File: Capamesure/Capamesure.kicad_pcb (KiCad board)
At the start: 2 copper layers, 75 x 48 mm, 61 parts, among them Q1 MMBT3904, Q2 MMBT3904, Q3 MMBT3906, Q4 MMBT3906, Q5 MMBT3904, Q6 MMBT3904, Q7 MMBT3904, U1 AZ1117-5.0

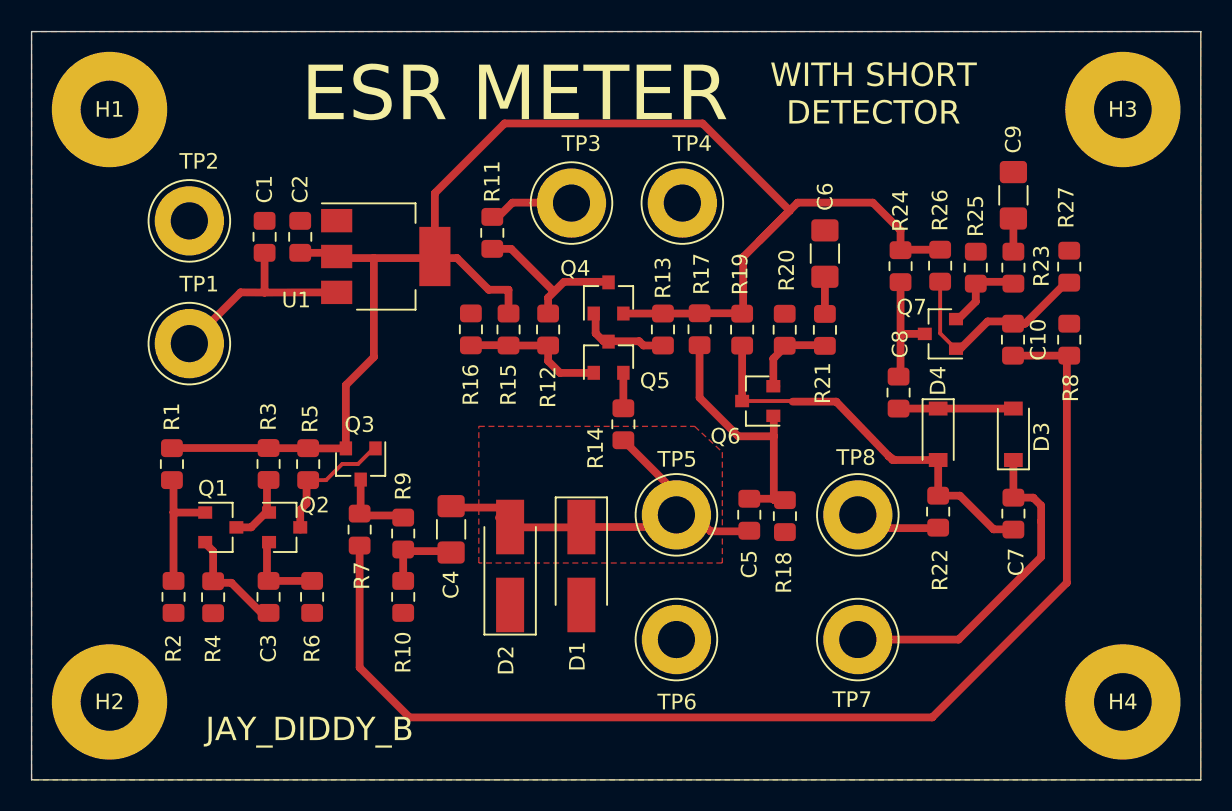
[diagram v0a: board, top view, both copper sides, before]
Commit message: Capacitor & Resistoir changes
changed footprint
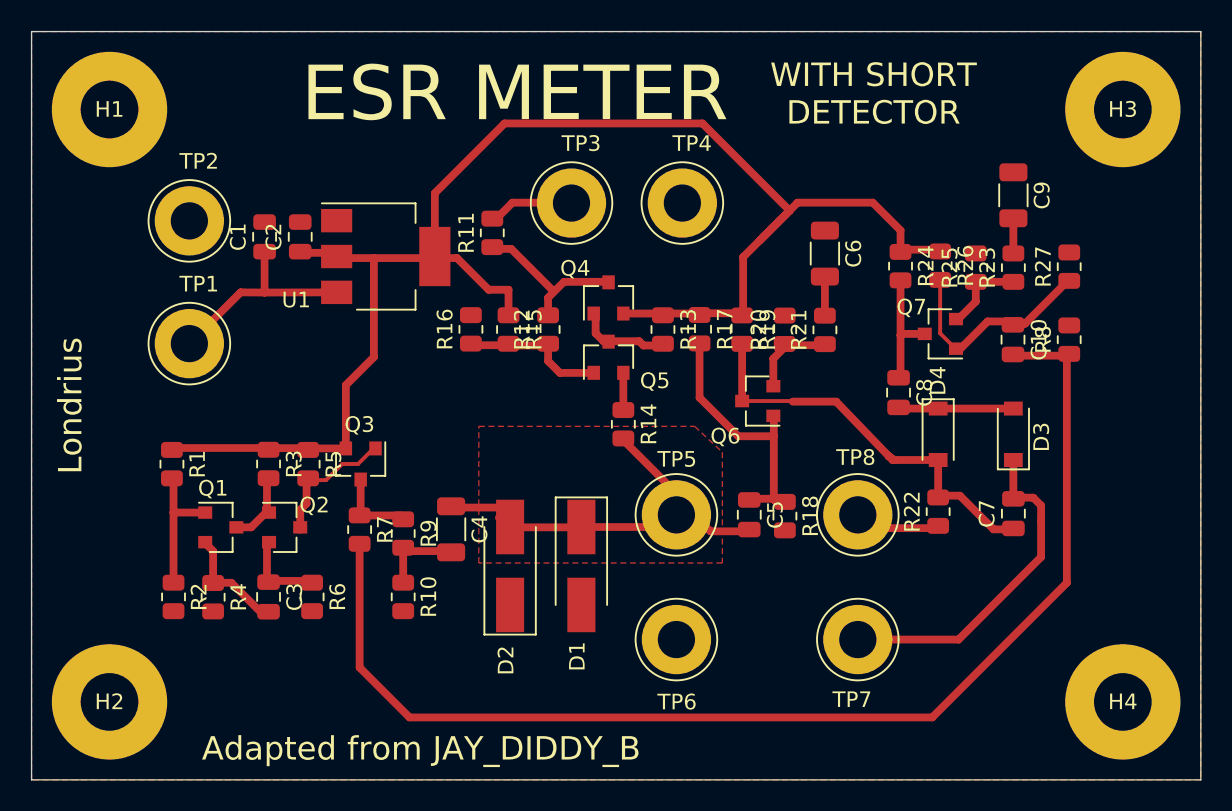
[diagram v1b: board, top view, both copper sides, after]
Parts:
- C1: value 100n -> 10u; footprint Capacitor_SMD:C_0805_2012Metric_Pad1.15x1.40mm_HandSolder -> Capacitor_SMD:C_0805_2012Metric
- C10, C3, C5, C7, C8: footprint Capacitor_SMD:C_0805_2012Metric_Pad1.15x1.40mm_HandSolder -> Capacitor_SMD:C_0805_2012Metric
- C2: value 100n -> 22u; footprint Capacitor_SMD:C_0805_2012Metric_Pad1.15x1.40mm_HandSolder -> Capacitor_SMD:C_0805_2012Metric
- C4, C6, C9: footprint Capacitor_SMD:C_1206_3216Metric_Pad1.42x1.75mm_HandSolder -> Capacitor_SMD:C_1206_3216Metric
- R1, R10, R11, R12, R13, R14, R15, R16, R17, R18, R19, R2, R20, R21, R22, R23, R24, R25, R26, R27, R3, R4, R5, R6, R7, R8, R9: footprint Resistor_SMD:R_0805_2012Metric_Pad1.15x1.40mm_HandSolder -> Resistor_SMD:R_0805_2012Metric
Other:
- board text added: "Adapted from JAY_DIDDY_B"
- board text added: "Londrius"
- board text removed: "JAY_DIDDY_B"
